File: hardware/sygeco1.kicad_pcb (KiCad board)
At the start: 2 copper layers, 30.5 x 73 mm, 19 parts, among them J1 SSD1306_module, J2 AVR-ISP-6, SW1 SW_Push_DPDT, SW2 SW_Push_DPDT, U1 ATtiny85-20PU

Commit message: cleaning
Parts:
- moved REF** 5.02 mm to (90.6, 71.5)
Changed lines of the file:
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@@
     (thickness 1.6)
     (drawings 21)
-    (tracks 192)
+    (tracks 191)
     (zones 0)
     (modules 19)
@@
     (pad 2 thru_hole circle (at 23.25 -0.05) (size 3 3) (drill 1.8) (layers *.Cu *.Mask)
       (net 2 GND))
-    (model "/home/orzel/hg/sygeco1/Coin Cell Holder CR2025 & CR2032.stp"
+    (model ${KIPRJMOD}/3dmodels/ChineseCR2032Holder.stp
       (offset (xyz 3 0 1))
       (scale (xyz 1 1 1))
@@
   )
   (module Display:Adafruit_SSD1306 (layer F.Cu)
-    (at 88.773 66.802)
+    (at 90.551 71.501)
     (descr "Adafruit SSD1306 OLED 1.3 inch 128x64 I2C & SPI https://learn.adafruit.com/monochrome-oled-breakouts/downloads")
     (tags "Adafruit SSD1306 OLED 1.3 inch 128x64 I2C & SPI ")
@@
       (effects (font (size 1 1) (thickness 0.15)) (justify mirror))
     )
-    (fp_text user %R (at 0 0 90) (layer B.Fab)
-      (effects (font (size 0.8 0.8) (thickness 0.12)) (justify mirror))
-    )
     (fp_line (start -1.6 -0.8) (end -1.6 0.8) (layer B.Fab) (width 0.1))
     (fp_line (start -1.6 0.8) (end 1.6 0.8) (layer B.Fab) (width 0.1))
@@
     (fp_line (start 2.45 1.12) (end 2.45 -1.12) (layer B.CrtYd) (width 0.05))
     (fp_line (start 2.45 -1.12) (end -2.45 -1.12) (layer B.CrtYd) (width 0.05))
+    (fp_text user %R (at 0 0 90) (layer B.Fab)
+      (effects (font (size 0.8 0.8) (thickness 0.12)) (justify mirror))
+    )
     (pad 2 smd roundrect (at 1.55 0 90) (size 1.3 1.75) (layers B.Cu B.Paste B.Mask) (roundrect_rratio 0.192308)
       (net 9 Button))
@@
     (fp_text value 50k (at 0 -1.82 90) (layer B.Fab)
       (effects (font (size 1 1) (thickness 0.15)) (justify mirror))
-    )
-    (fp_text user %R (at 0 0 90) (layer B.Fab)
-      (effects (font (size 0.8 0.8) (thickness 0.12)) (justify mirror))
     )
     (fp_line (start -1.6 -0.8) (end -1.6 0.8) (layer B.Fab) (width 0.1))
@@
     (fp_line (start 2.45 1.12) (end 2.45 -1.12) (layer B.CrtYd) (width 0.05))
     (fp_line (start 2.45 -1.12) (end -2.45 -1.12) (layer B.CrtYd) (width 0.05))
+    (fp_text user %R (at 0 0 90) (layer B.Fab)
+      (effects (font (size 0.8 0.8) (thickness 0.12)) (justify mirror))
+    )
     (pad 2 smd roundrect (at 1.55 0 270) (size 1.3 1.75) (layers B.Cu B.Paste B.Mask) (roundrect_rratio 0.192308)
       (net 10 PAD_AXE_2))
@@
   (via (at 144.78 64.008) (size 0.8) (drill 0.4) (layers F.Cu B.Cu) (net 2))
   (segment (start 144.78 64.008) (end 141.986 64.008) (width 0.25) (layer F.Cu) (net 2))
-  (segment (start 140.97 62.992) (end 141.986 64.008) (width 0.25) (layer F.Cu) (net 2))
-  (segment (start 140.97 61.595) (end 140.97 62.992) (width 0.25) (layer F.Cu) (net 2))
   (segment (start 144.272 112.776) (end 144.272 112.776) (width 0.25) (layer B.Cu) (net 2))
   (segment (start 144.272 119.38) (end 145.438 120.546) (width 0.25) (layer B.Cu) (net 2))
@@
   (segment (start 150.418 83.77) (end 146.408 87.78) (width 0.25) (layer B.Cu) (net 2))
   (segment (start 152.79 83.77) (end 150.418 83.77) (width 0.25) (layer B.Cu) (net 2))
-  (segment (start 131.572 69.088) (end 130.556 70.104) (width 0.25) (layer F.Cu) (net 2))
-  (segment (start 131.572 67.564) (end 131.572 69.088) (width 0.25) (layer F.Cu) (net 2))
-  (segment (start 138.176 66.04) (end 133.096 66.04) (width 0.25) (layer F.Cu) (net 2))
-  (segment (start 133.096 66.04) (end 131.572 67.564) (width 0.25) (layer F.Cu) (net 2))
-  (segment (start 140.97 63.246) (end 138.176 66.04) (width 0.25) (layer F.Cu) (net 2))
-  (segment (start 140.97 62.992) (end 140.97 63.246) (width 0.25) (layer F.Cu) (net 2))
   (segment (start 132.3725 106.9725) (end 132.3725 108.966) (width 0.25) (layer B.Cu) (net 2))
   (segment (start 131.064 105.664) (end 132.3725 106.9725) (width 0.25) (layer B.Cu) (net 2))
@@
   (segment (start 146.408 106.322) (end 146.408 102.108) (width 0.25) (layer F.Cu) (net 2))
   (segment (start 143.764 108.966) (end 146.408 106.322) (width 0.25) (layer F.Cu) (net 2))
+  (segment (start 140.97 64.008) (end 140.97 61.595) (width 0.25) (layer F.Cu) (net 2))
+  (segment (start 138.938 66.04) (end 140.97 64.008) (width 0.25) (layer F.Cu) (net 2))
+  (segment (start 133.096 66.04) (end 138.938 66.04) (width 0.25) (layer F.Cu) (net 2))
+  (segment (start 131.572 67.564) (end 133.096 66.04) (width 0.25) (layer F.Cu) (net 2))
+  (segment (start 131.572 69.088) (end 131.572 67.564) (width 0.25) (layer F.Cu) (net 2))
+  (segment (start 130.556 70.104) (end 131.572 69.088) (width 0.25) (layer F.Cu) (net 2))
+  (segment (start 141.986 64.008) (end 140.97 64.008) (width 0.25) (layer F.Cu) (net 2))
   (segment (start 130.556 72.644) (end 128.524 72.644) (width 0.25) (layer B.Cu) (net 3))
   (segment (start 128.524 72.644) (end 128.524 79.248) (width 0.25) (layer B.Cu) (net 3))

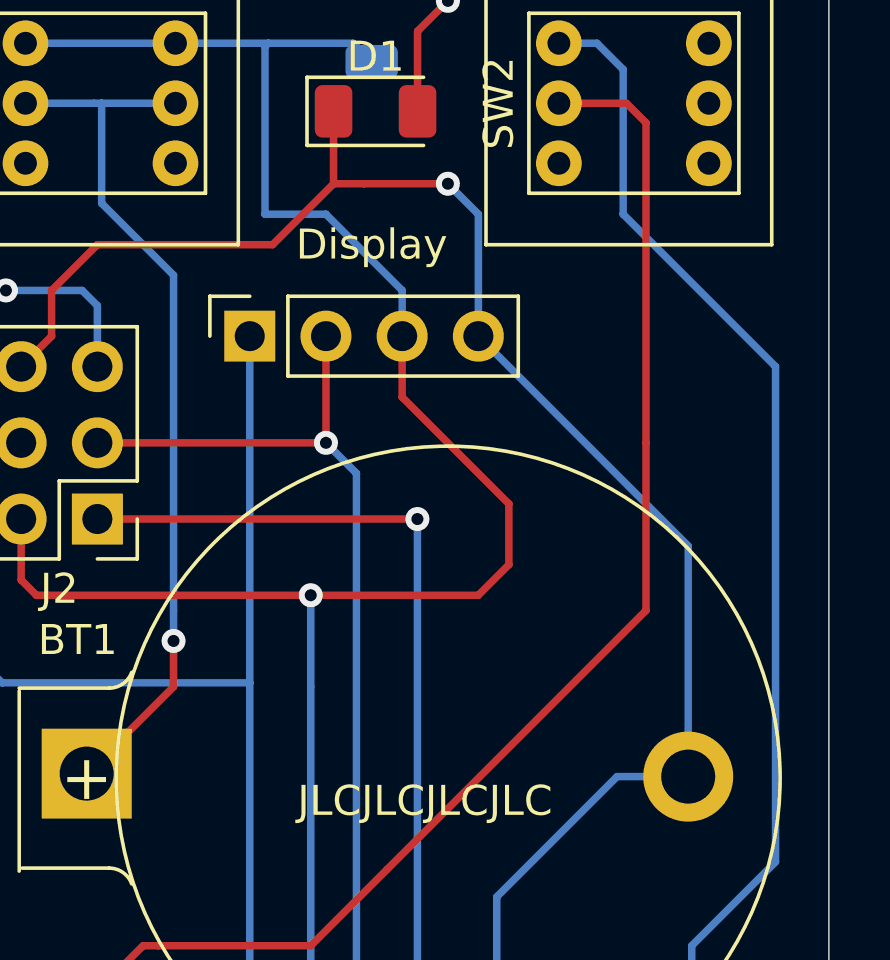
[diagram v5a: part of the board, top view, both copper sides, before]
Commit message: oops, the oled connector position was inversed, fixed that
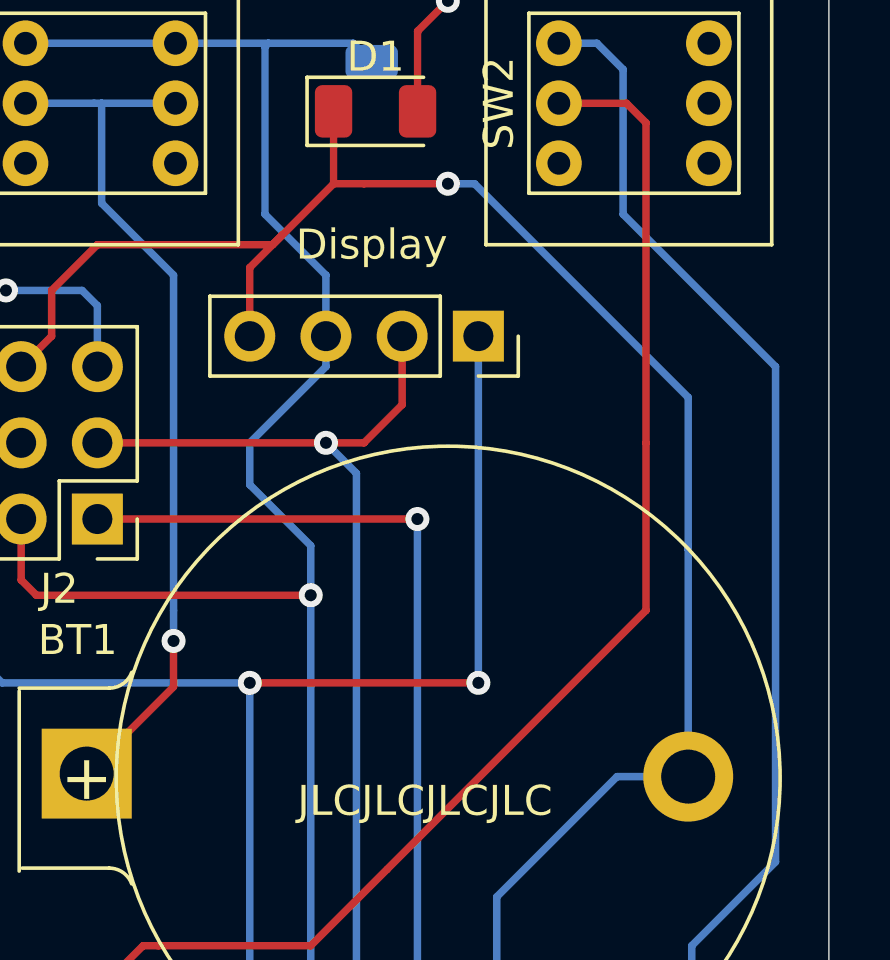
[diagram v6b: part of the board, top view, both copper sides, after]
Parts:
- moved J1 7.62 mm to (145.8, 69.1), turned to 270 degrees
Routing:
- net VCC: track 141.4 -> 133.6 mm
- net SDA: track 57.8 -> 65.5 mm, vias 0 -> 2
- net GND: track 104.6 -> 109.1 mm
- net SCL: track 41.2 -> 43.0 mm
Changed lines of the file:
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@@
     (thickness 1.6)
     (drawings 21)
-    (tracks 191)
+    (tracks 201)
     (zones 0)
     (modules 19)
@@
   )
   (module Connector_PinSocket_2.54mm:PinSocket_1x04_P2.54mm_Vertical (layer F.Cu)
-    (at 138.176 69.088 90)
+    (at 145.796 69.088 270)
     (descr "Through hole straight socket strip, 1x04, 2.54mm pitch, single row (from Kicad 4.0.7), script generated")
     (tags "Through hole socket strip THT 1x04 2.54mm single row")
@@
       (effects (font (size 1 1) (thickness 0.15)))
     )
-    (pad 1 thru_hole rect (at 0 0 90) (size 1.7 1.7) (drill 1) (layers *.Cu *.Mask)
+    (pad 1 thru_hole rect (at 0 0 270) (size 1.7 1.7) (drill 1) (layers *.Cu *.Mask)
       (net 3 SDA))
-    (pad 2 thru_hole oval (at 0 2.54 90) (size 1.7 1.7) (drill 1) (layers *.Cu *.Mask)
+    (pad 2 thru_hole oval (at 0 2.54 270) (size 1.7 1.7) (drill 1) (layers *.Cu *.Mask)
       (net 4 SCL))
-    (pad 3 thru_hole oval (at 0 5.08 90) (size 1.7 1.7) (drill 1) (layers *.Cu *.Mask)
+    (pad 3 thru_hole oval (at 0 5.08 270) (size 1.7 1.7) (drill 1) (layers *.Cu *.Mask)
       (net 5 VCC))
-    (pad 4 thru_hole oval (at 0 7.62 90) (size 1.7 1.7) (drill 1) (layers *.Cu *.Mask)
+    (pad 4 thru_hole oval (at 0 7.62 270) (size 1.7 1.7) (drill 1) (layers *.Cu *.Mask)
       (net 2 GND))
     (model ${KISYS3DMOD}/Connector_PinSocket_2.54mm.3dshapes/PinSocket_1x04_P2.54mm_Vertical.wrl
@@
   (segment (start 135.636 80.774) (end 132.74 83.67) (width 0.25) (layer F.Cu) (net 1))
   (segment (start 135.636 79.248) (end 135.636 80.774) (width 0.25) (layer F.Cu) (net 1))
-  (segment (start 152.79 76.082) (end 145.796 69.088) (width 0.25) (layer B.Cu) (net 2))
-  (segment (start 152.79 83.77) (end 152.79 76.082) (width 0.25) (layer B.Cu) (net 2))
-  (segment (start 145.796 69.088) (end 145.796 65.024) (width 0.25) (layer B.Cu) (net 2))
-  (segment (start 145.796 65.024) (end 144.78 64.008) (width 0.25) (layer B.Cu) (net 2))
   (segment (start 144.78 64.008) (end 144.78 64.008) (width 0.25) (layer B.Cu) (net 2))
   (via (at 144.78 64.008) (size 0.8) (drill 0.4) (layers F.Cu B.Cu) (net 2))
@@
   (segment (start 143.764 108.966) (end 146.408 106.322) (width 0.25) (layer F.Cu) (net 2))
   (segment (start 140.97 64.008) (end 140.97 61.595) (width 0.25) (layer F.Cu) (net 2))
-  (segment (start 138.938 66.04) (end 140.97 64.008) (width 0.25) (layer F.Cu) (net 2))
   (segment (start 133.096 66.04) (end 138.938 66.04) (width 0.25) (layer F.Cu) (net 2))
   (segment (start 131.572 67.564) (end 133.096 66.04) (width 0.25) (layer F.Cu) (net 2))
@@
   (segment (start 130.556 70.104) (end 131.572 69.088) (width 0.25) (layer F.Cu) (net 2))
   (segment (start 141.986 64.008) (end 140.97 64.008) (width 0.25) (layer F.Cu) (net 2))
+  (segment (start 138.176 66.802) (end 139.2555 65.7225) (width 0.25) (layer F.Cu) (net 2))
+  (segment (start 138.176 69.088) (end 138.176 66.802) (width 0.25) (layer F.Cu) (net 2))
+  (segment (start 139.2555 65.7225) (end 140.97 64.008) (width 0.25) (layer F.Cu) (net 2))
+  (segment (start 138.938 66.04) (end 139.2555 65.7225) (width 0.25) (layer F.Cu) (net 2))
+  (segment (start 144.78 64.008) (end 145.669 64.008) (width 0.25) (layer B.Cu) (net 2))
+  (segment (start 152.79 71.129) (end 152.79 76.191) (width 0.25) (layer B.Cu) (net 2))
+  (segment (start 145.669 64.008) (end 152.79 71.129) (width 0.25) (layer B.Cu) (net 2))
+  (segment (start 152.79 76.191) (end 152.79 76.082) (width 0.25) (layer B.Cu) (net 2))
+  (segment (start 152.79 83.77) (end 152.79 76.191) (width 0.25) (layer B.Cu) (net 2))
   (segment (start 130.556 72.644) (end 128.524 72.644) (width 0.25) (layer B.Cu) (net 3))
   (segment (start 128.524 72.644) (end 128.524 79.248) (width 0.25) (layer B.Cu) (net 3))
@@
   (segment (start 129.921 80.645) (end 128.524 79.248) (width 0.25) (layer B.Cu) (net 3))
   (segment (start 138.176 80.645) (end 129.921 80.645) (width 0.25) (layer B.Cu) (net 3))
-  (segment (start 138.176 69.088) (end 138.176 80.645) (width 0.25) (layer B.Cu) (net 3))
+  (segment (start 138.176 80.645) (end 138.176 80.645) (width 0.25) (layer B.Cu) (net 3))
+  (segment (start 145.796 69.088) (end 145.796 80.645) (width 0.25) (layer B.Cu) (net 3))
+  (segment (start 145.796 80.645) (end 145.796 80.645) (width 0.25) (layer B.Cu) (net 3))
+  (via (at 145.796 80.645) (size 0.8) (drill 0.4) (layers F.Cu B.Cu) (net 3))
   (segment (start 138.176 80.645) (end 138.176 90.932) (width 0.25) (layer B.Cu) (net 3))
+  (via (at 138.176 80.645) (size 0.8) (drill 0.4) (layers F.Cu B.Cu) (net 3))
+  (segment (start 145.796 80.645) (end 138.176 80.645) (width 0.25) (layer F.Cu) (net 3))
   (via (at 140.716 72.644) (size 0.8) (drill 0.4) (layers F.Cu B.Cu) (net 4))
   (segment (start 133.096 72.644) (end 140.716 72.644) (width 0.25) (layer F.Cu) (net 4))
-  (segment (start 140.716 69.088) (end 140.716 72.644) (width 0.25) (layer F.Cu) (net 4))
   (segment (start 141.732 98.552) (end 140.208 100.076) (width 0.25) (layer B.Cu) (net 4))
   (segment (start 140.208 100.076) (end 138.684 100.076) (width 0.25) (layer B.Cu) (net 4))
   (segment (start 141.732 73.66) (end 141.732 98.552) (width 0.25) (layer B.Cu) (net 4))
   (segment (start 140.716 72.644) (end 141.732 73.66) (width 0.25) (layer B.Cu) (net 4))
+  (segment (start 143.256 69.088) (end 143.256 71.374) (width 0.25) (layer F.Cu) (net 4))
+  (segment (start 141.986 72.644) (end 140.716 72.644) (width 0.25) (layer F.Cu) (net 4))
+  (segment (start 143.256 71.374) (end 141.986 72.644) (width 0.25) (layer F.Cu) (net 4))
   (segment (start 135.7 59.325) (end 130.7 59.325) (width 0.25) (layer B.Cu) (net 5))
   (segment (start 141.621 59.325) (end 142.24 59.944) (width 0.25) (layer B.Cu) (net 5))
   (segment (start 138.684 59.436) (end 138.795 59.325) (width 0.25) (layer B.Cu) (net 5))
   (segment (start 138.684 65.024) (end 138.684 59.436) (width 0.25) (layer B.Cu) (net 5))
-  (segment (start 140.716 65.024) (end 138.684 65.024) (width 0.25) (layer B.Cu) (net 5))
-  (segment (start 143.256 67.564) (end 140.716 65.024) (width 0.25) (layer B.Cu) (net 5))
   (segment (start 138.795 59.325) (end 141.621 59.325) (width 0.25) (layer B.Cu) (net 5))
-  (segment (start 143.256 69.088) (end 143.256 67.564) (width 0.25) (layer B.Cu) (net 5))
   (segment (start 135.7 59.325) (end 138.795 59.325) (width 0.25) (layer B.Cu) (net 5))
   (segment (start 147.32 97.536) (end 149.86 100.076) (width 0.25) (layer F.Cu) (net 5))
@@
   (segment (start 138.684 96.52) (end 140.208 94.996) (width 0.25) (layer B.Cu) (net 5))
   (segment (start 138.684 97.536) (end 138.684 96.52) (width 0.25) (layer B.Cu) (net 5))
-  (segment (start 145.796 77.724) (end 140.208 77.724) (width 0.25) (layer F.Cu) (net 5))
-  (segment (start 146.812 76.708) (end 145.796 77.724) (width 0.25) (layer F.Cu) (net 5))
-  (segment (start 143.256 71.12) (end 146.812 74.676) (width 0.25) (layer F.Cu) (net 5))
-  (segment (start 146.812 74.676) (end 146.812 76.708) (width 0.25) (layer F.Cu) (net 5))
-  (segment (start 143.256 69.088) (end 143.256 71.12) (width 0.25) (layer F.Cu) (net 5))
   (segment (start 154.7475 115.7625) (end 152.4 115.7625) (width 0.25) (layer B.Cu) (net 5))
   (segment (start 155.448 115.062) (end 154.7475 115.7625) (width 0.25) (layer B.Cu) (net 5))
@@
   (segment (start 128.524 108.2425) (end 129.2475 108.966) (width 0.25) (layer B.Cu) (net 5))
   (segment (start 128.524 93.98) (end 128.524 108.2425) (width 0.25) (layer B.Cu) (net 5))
+  (segment (start 140.716 67.056) (end 138.684 65.024) (width 0.25) (layer B.Cu) (net 5))
+  (segment (start 140.716 69.088) (end 140.716 67.056) (width 0.25) (layer B.Cu) (net 5))
+  (segment (start 140.208 76.073) (end 140.208 77.724) (width 0.25) (layer B.Cu) (net 5))
+  (segment (start 138.176 74.041) (end 140.208 76.073) (width 0.25) (layer B.Cu) (net 5))
+  (segment (start 138.176 72.644) (end 138.176 74.041) (width 0.25) (layer B.Cu) (net 5))
+  (segment (start 140.716 70.104) (end 138.176 72.644) (width 0.25) (layer B.Cu) (net 5))
+  (segment (start 140.716 69.088) (end 140.716 70.104) (width 0.25) (layer B.Cu) (net 5))
   (segment (start 152.908 89.408) (end 152.908 102.108) (width 0.25) (layer B.Cu) (net 6))
   (segment (start 155.702 86.614) (end 152.908 89.408) (width 0.25) (layer B.Cu) (net 6))

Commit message: cleaning / small improvements
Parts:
- removed the REF** at (90.6, 71.5)
- added REF**: PinHeader_1x04_P2.54mm_Vertical, Connector_PinHeader_2.54mm:PinHeader_1x04_P2.54mm_Vertical, F.Cu at (112.9, 69.6)
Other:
- board text added: "GND"
- board text added: "ISP"
- board text added: "Vcc"

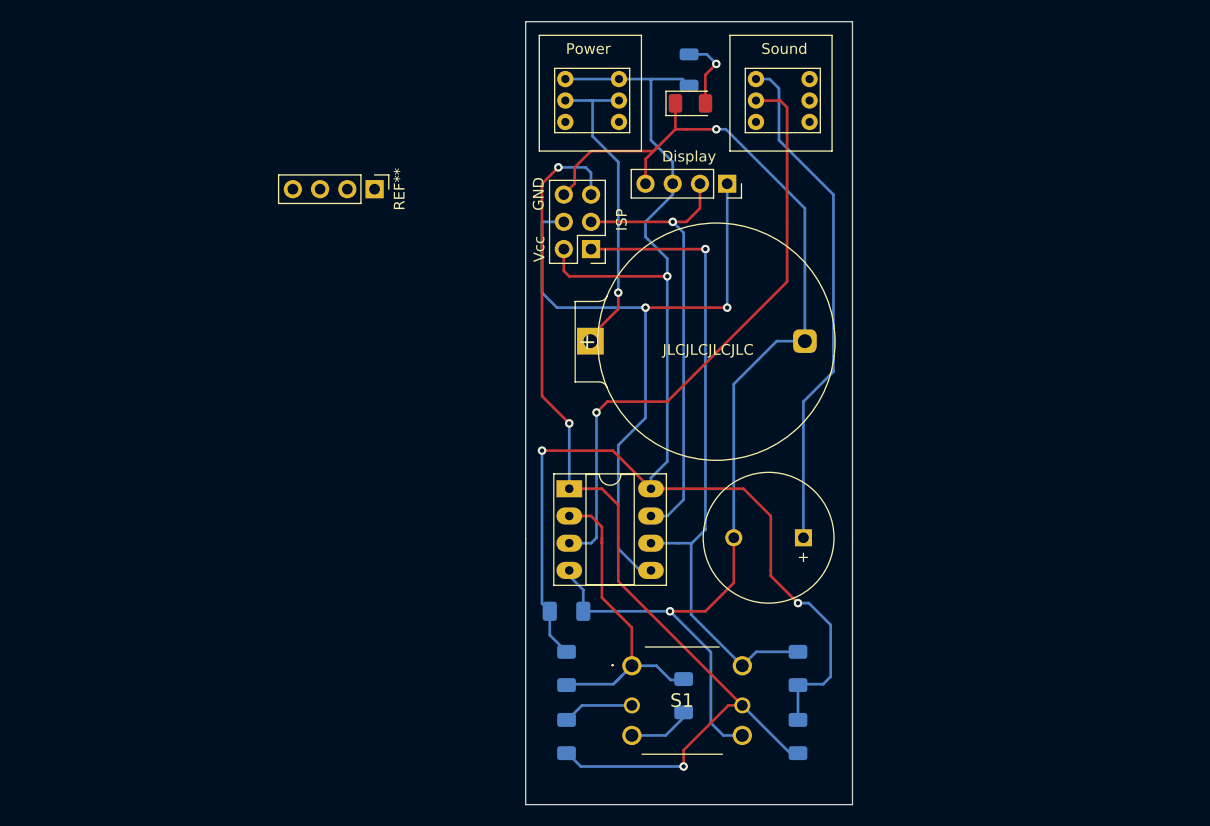
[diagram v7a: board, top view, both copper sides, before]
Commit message: few fixes * sch: fix typo (axe -> axis) * reduce battery holder hole size now that i have the actual device to check * some routing cleaning * contrary to my expectation, the isp header works as is, even with my large connector
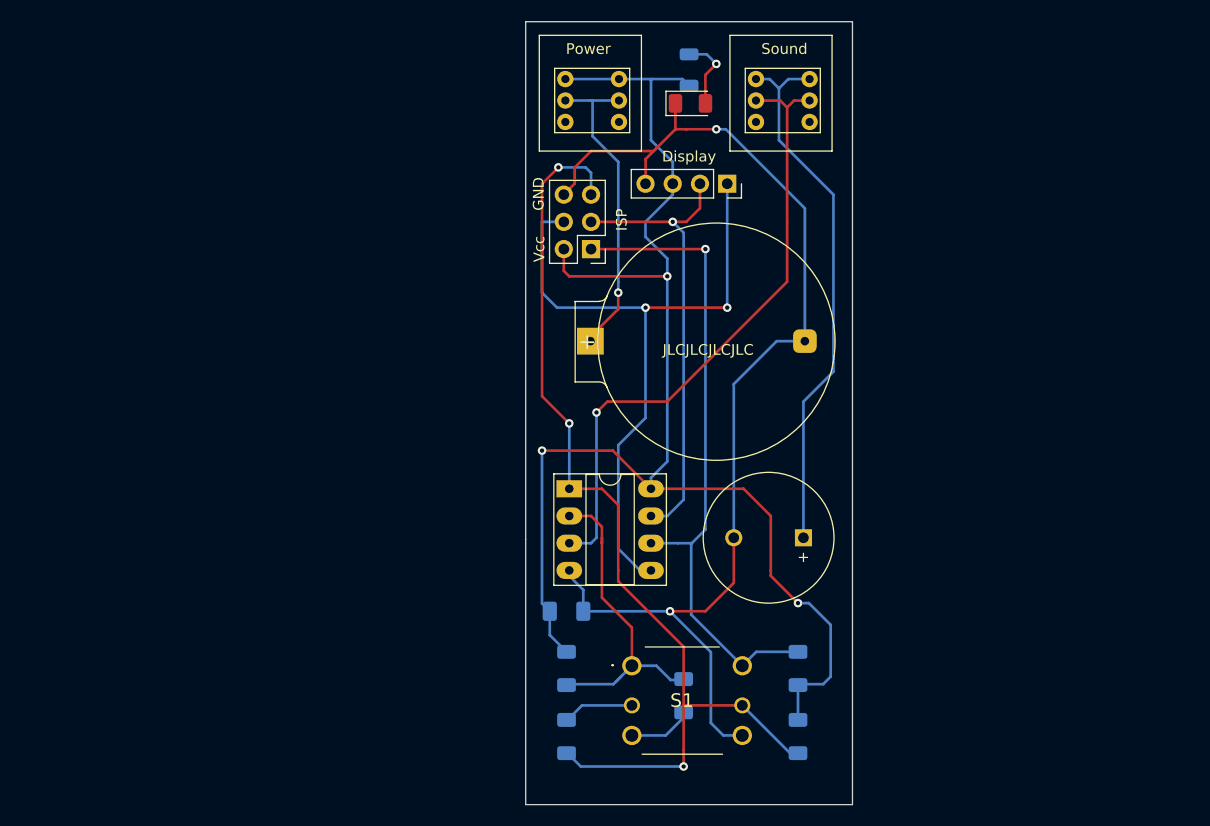
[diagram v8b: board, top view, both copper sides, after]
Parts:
- removed G***: LOGO, sygeco:Sylphide_logo
- removed REF**: PinHeader_1x04_P2.54mm_Vertical, Connector_PinHeader_2.54mm:PinHeader_1x04_P2.54mm_Vertical
- removed REF**: OSHW-Logo2_7.3x6mm_SilkScreen, Symbol:OSHW-Logo2_7.3x6mm_SilkScreen
- R6: value 15 -> 60~100
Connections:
- net PAD_AXE_1 renamed PAD_AXIS_1
- net PAD_AXE_2 renamed PAD_AXIS_2
- SW2 pad 5: Net-(SW2-Pad5) -> Net-(SW2-Pad2)
- SW2 pad 6: Net-(SW2-Pad6) -> Net-(LS1-Pad1)
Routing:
- net Net-(LS1-Pad1): track 47.7 -> 50.9 mm
- net Net-(SW2-Pad2): track 56.7 -> 59.1 mm
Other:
- board text added: "Version 0.2"
- board text removed: "Version 0.1"
